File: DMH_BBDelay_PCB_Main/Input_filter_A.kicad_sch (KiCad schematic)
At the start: 18 parts, among them U21 TL072

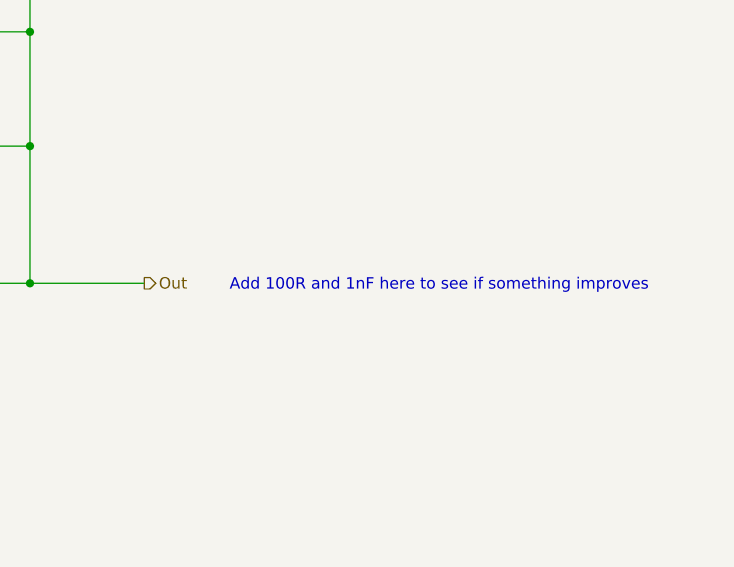
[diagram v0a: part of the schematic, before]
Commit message: Added clamping to compressors outputs
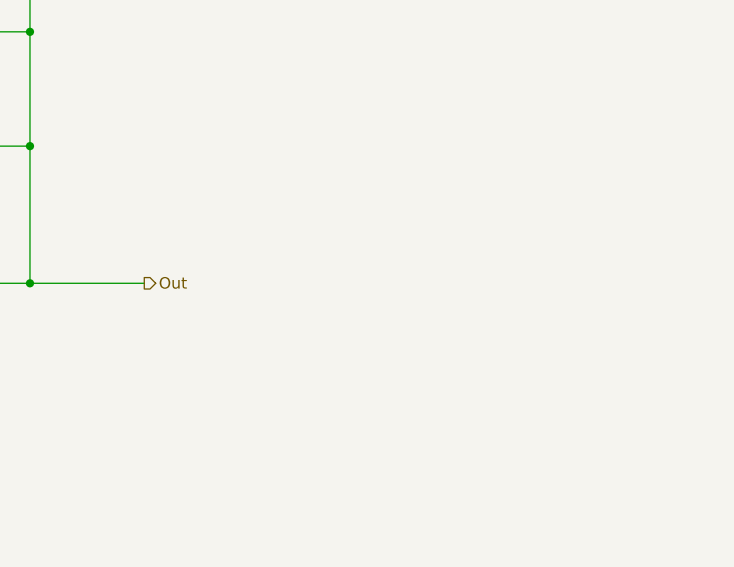
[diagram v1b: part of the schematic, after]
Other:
- note removed: "Add 100R and 1nF here to see if something improves"
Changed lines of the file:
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@@
 		(comment 1 "PCB for 10cm Kosmo format synthesizer module")
-	)
-	(text "Add 100R and 1nF here to see if something improves"
-		(exclude_from_sim no)
-		(at 185.166 66.294 0)
-		(effects
-			(font
-				(size 1.27 1.27)
-			)
-		)
 	)
 	(junction

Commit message: Made feedback work
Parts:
- added D33, D34: 1N4148, Diode_THT:D_DO-35_SOD27_P7.62mm_Horizontal, symbol Diode:1N4148
- added R249: 1k, Resistor_THT:R_Axial_DIN0207_L6.3mm_D2.5mm_P7.62mm_Horizontal, symbol Device:R_US
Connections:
- net GND: now also D33.2 (A), D34.1 (K)
- net In: now also R249.1; no longer C112.1, R6.2
- new net: C112.1, D33.1 (K), D34.2 (A), R249.2, R6.2
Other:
- moved on the sheet: C110, C112, C55, C56, C57, C58, C59, C60, R158, R159, R177, R178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

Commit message: Synced channel A and B schematics
... and applied several minor improvements and optimizations.
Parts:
- removed C112: 3.3uF, Capacitor_THT:C_Disc_D4.3mm_W1.9mm_P5.00mm, symbol Device:C
- removed C56: 47p, Capacitor_THT:C_Disc_D3.0mm_W2.0mm_P2.50mm, symbol Device:C
- removed C58: 470p, Capacitor_THT:C_Disc_D3.0mm_W2.0mm_P2.50mm, symbol Device:C
- C55: value 100p -> 150p
- C57, C60: value 1nF -> 1.5nF
- C59: value 470p -> 1uF Film; footprint Capacitor_THT:C_Disc_D3.0mm_W2.0mm_P2.50mm -> Capacitor_THT:C_Disc_D7.5mm_W5.0mm_P5.00mm
- R41: value 22k -> 20k
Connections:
- net GND: no longer C59.1
- net at C60.2, R158.2, R159.1: no longer C59.2
- net at D33.1 (K), D34.2 (A), R249.2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: now also C59.1
- net at R158.1: now also C59.2

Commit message: Perfected circuit with double V3205
Next step is try quad V3205 per channel to reduce aliasing further
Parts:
- R42: value 22k -> 20k
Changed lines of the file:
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@@
 			)
 		)
-		(property "Value" "22k"
+		(property "Value" "20k"
 			(at 149.86 109.2199 0)
 			(show_name no)
